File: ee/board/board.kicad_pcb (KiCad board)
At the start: 4 copper layers, 87.1 x 53.4 mm, 103 parts, among them J3 USB_A, J4 Conn_01x08_Pin, J5 Conn_01x10_Pin, J6 Conn_Coaxial, J8 HR911105A, U1 RTL8201F, U2 RTL8723DS, U6 USBLC6-2SC6, Y1 Crystal_GND24_Small

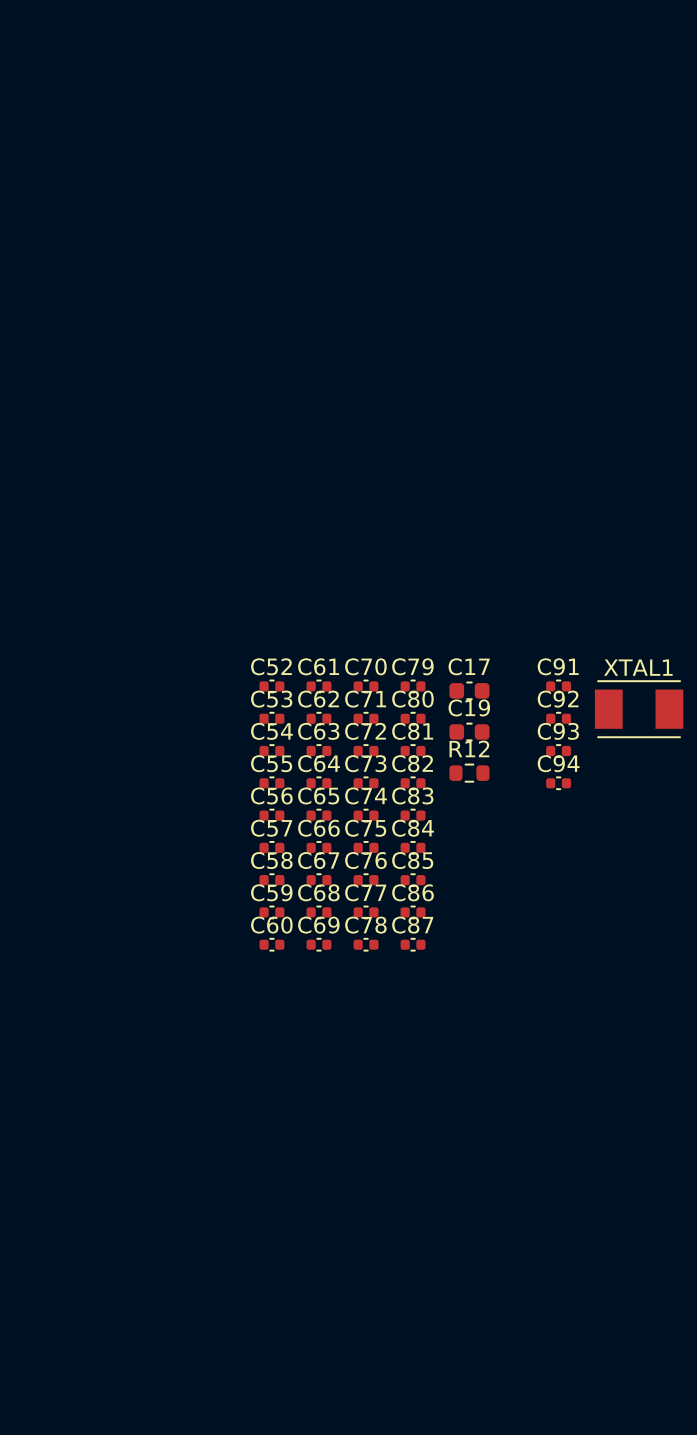
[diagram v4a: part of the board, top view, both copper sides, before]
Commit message: Added the footprints into the design.
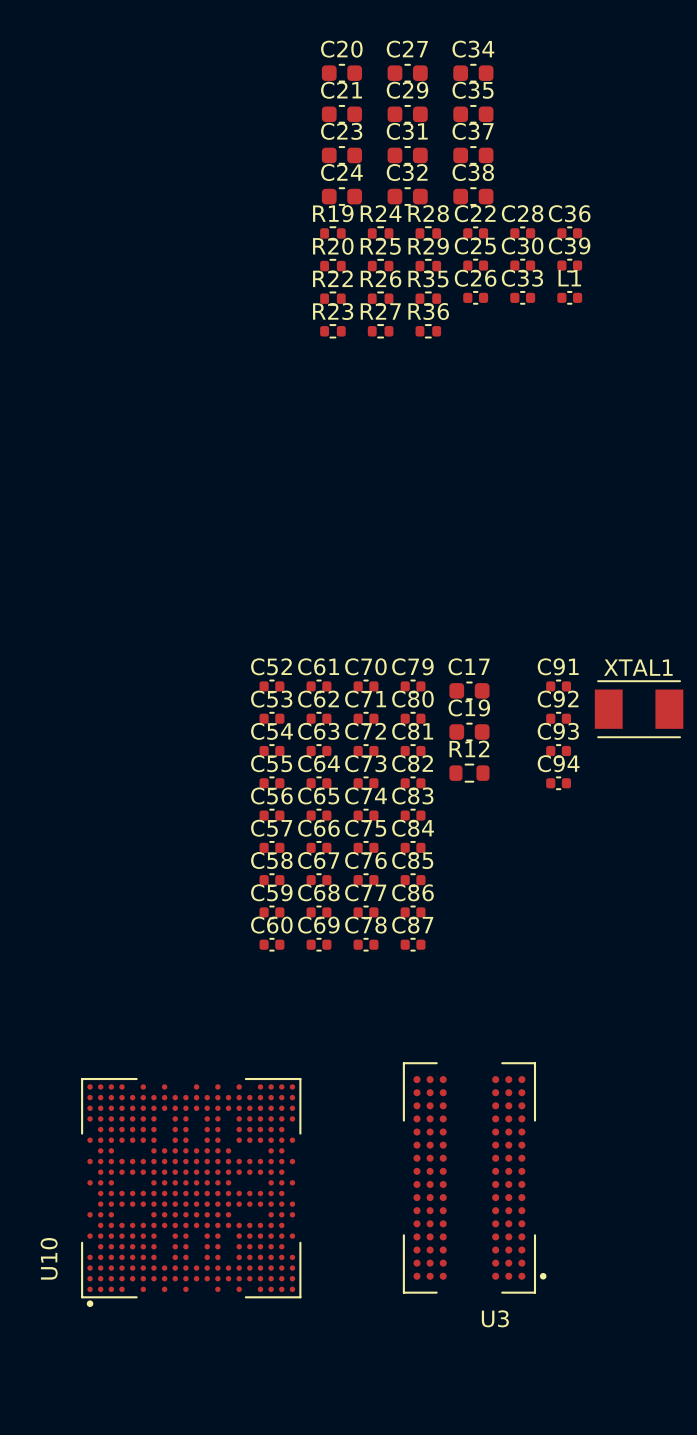
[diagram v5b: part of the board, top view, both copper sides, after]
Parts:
- added C20: 22uF, Capacitor_SMD:C_0603_1608Metric, F.Cu at (72.7, 64.9)
- added C21: 10uF, Capacitor_SMD:C_0603_1608Metric, F.Cu at (72.7, 67.4)
- added C22: 0.1uF, Capacitor_SMD:C_0402_1005Metric, F.Cu at (80.9, 74.7)
- added C23: 10uF, Capacitor_SMD:C_0603_1608Metric, F.Cu at (72.7, 69.9)
- added C24: 10uF, Capacitor_SMD:C_0603_1608Metric, F.Cu at (72.7, 72.4)
- added C25: 0.1uF, Capacitor_SMD:C_0402_1005Metric, F.Cu at (80.9, 76.6)
- added C26: 0.1uF, Capacitor_SMD:C_0402_1005Metric, F.Cu at (80.9, 78.6)
- added C27: 10uF, Capacitor_SMD:C_0603_1608Metric, F.Cu at (76.7, 64.9)
- added C28: 0.1uF, Capacitor_SMD:C_0402_1005Metric, F.Cu at (83.8, 74.7)
- added C29: 22uF, Capacitor_SMD:C_0603_1608Metric, F.Cu at (76.7, 67.4)
- added C30: 0.1uF, Capacitor_SMD:C_0402_1005Metric, F.Cu at (83.8, 76.6)
- added C31: 22uF, Capacitor_SMD:C_0603_1608Metric, F.Cu at (76.7, 69.9)
- added C32: 22uF, Capacitor_SMD:C_0603_1608Metric, F.Cu at (76.7, 72.4)
- added C33: 0.1uF, Capacitor_SMD:C_0402_1005Metric, F.Cu at (83.8, 78.6)
- added C34: 22uF, Capacitor_SMD:C_0603_1608Metric, F.Cu at (80.7, 64.9)
- added C35: 22uF, Capacitor_SMD:C_0603_1608Metric, F.Cu at (80.7, 67.4)
- added C36: 0.1uF, Capacitor_SMD:C_0402_1005Metric, F.Cu at (86.6, 74.7)
- added C37: 22uF, Capacitor_SMD:C_0603_1608Metric, F.Cu at (80.7, 69.9)
- added C38: 22uF, Capacitor_SMD:C_0603_1608Metric, F.Cu at (80.7, 72.4)
- added C39: 0.1uF, Capacitor_SMD:C_0402_1005Metric, F.Cu at (86.6, 76.6)
- added L1: 3.3uH, Capacitor_SMD:C_0402_1005Metric, F.Cu at (86.6, 78.6)
- added R19: 10k, Resistor_SMD:R_0402_1005Metric, F.Cu at (72.2, 74.7)
- added R20: 590R, Resistor_SMD:R_0402_1005Metric, F.Cu at (72.2, 76.7)
- added R22: 10k, Resistor_SMD:R_0402_1005Metric, F.Cu at (72.2, 78.7)
- added R23: 31.6k, Resistor_SMD:R_0402_1005Metric, F.Cu at (72.2, 80.6)
- added R24: 10k, Resistor_SMD:R_0402_1005Metric, F.Cu at (75.1, 74.7)
- added R25: 10k, Resistor_SMD:R_0402_1005Metric, F.Cu at (75.1, 76.7)
- added R26: 8.66K, Resistor_SMD:R_0402_1005Metric, F.Cu at (75.1, 78.7)
- added R27: 10k, Resistor_SMD:R_0402_1005Metric, F.Cu at (75.1, 80.6)
- added R28: 10k, Resistor_SMD:R_0402_1005Metric, F.Cu at (78.0, 74.7)
- added R29: 10k, Resistor_SMD:R_0402_1005Metric, F.Cu at (78.0, 76.7)
- added R35: 12.4K, Resistor_SMD:R_0402_1005Metric, F.Cu at (78.0, 78.7)
- added R36: 10k, Resistor_SMD:R_0402_1005Metric, F.Cu at (78.0, 80.6)
- added U10: ALLWINNER_D1, allwinnder_d1:BGA337C65P20X20_1300X1300X133, F.Cu at (63.5, 132.9)
- added U3: MT41K256M16TW-107_P, ddr3:BGA96C80P9X16_1400X800X120, F.Cu at (80.5, 132.3)
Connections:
- net /MPU/PG12 renamed /MPU/PG10

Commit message: Leftover stuff
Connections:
- net /1W renamed /Flipper_1W
- net /B2 renamed /Flipper_B2
- net /B3 renamed /Flipper_B3
- net /C0 renamed /Flipper_C0
- net /C1 renamed /Flipper_C1
- net /C3 renamed /Flipper_C3
- net /SIO renamed /Flipper_SIO
- net /SWC renamed /Flipper_SWC
- J4 pad 2: /MPU/A7 -> /Flipper_A7
- J4 pad 3: /MPU/A6 -> /Flipper_A6
- J4 pad 4: /MPU/A4 -> /Flipper_A4
- JP1 pad 2: /MPU/PG18 -> /WiFi/PG18
- R14 pad 1: /MPU/PG11 -> /WiFi/PG11
- R16 pad 1: /MPU/PG7 -> /WiFi/PG7
- R17 pad 1: /MPU/PG6 -> /WiFi/PG6
- R18 pad 2: /MPU/PG10 -> /WiFi/PG10
- R4 pad 2: /MPU/PG16 -> /WiFi/PG16
- RN1 pad 1: /MPU/PG3 -> /WiFi/PG3
- RN1 pad 2: /MPU/PG2 -> /WiFi/PG2
- RN1 pad 3: /MPU/PG0 -> /WiFi/PG0
- RN1 pad 4: /MPU/PG1 -> /WiFi/PG1
- RN2 pad 1: /MPU/PG5 -> /WiFi/PG5
- RN2 pad 2: /MPU/PG4 -> /WiFi/PG4
- RN2 pad 3: /MPU/PG10 -> /WiFi/PG10
- RN2 pad 4: /MPU/PG10 -> /WiFi/PG10
- U10 pad D5: /MPU/PG10 -> /MPU/PG12
- U2 pad 12: /MPU/PG10 -> /WiFi/PG10
- U2 pad 13: /MPU/PG10 -> /WiFi/PG10
- U2 pad 14: /MPU/PG4 -> /WiFi/PG4
- U2 pad 15: /MPU/PG5 -> /WiFi/PG5
- U2 pad 16: /MPU/PG1 -> /WiFi/PG1
- U2 pad 17: /MPU/PG0 -> /WiFi/PG0
- U2 pad 18: /MPU/PG2 -> /WiFi/PG2
- U2 pad 19: /MPU/PG3 -> /WiFi/PG3
- U2 pad 41: /MPU/PG9 -> /WiFi/PG9
- U2 pad 44: /MPU/PG8 -> /WiFi/PG8
- U2 pad 6: /MPU/PG16 -> /WiFi/PG16
- U2 pad 7: /MPU/PG17 -> /WiFi/PG17
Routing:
- net /WiFi/PG10: track 0.00 -> 53.5 mm, vias 0 -> 4
- net /MPU/PG10: track 53.5 -> 0.00 mm, vias 4 -> 0
- net /WiFi/PG4: track 0.00 -> 30.0 mm, vias 0 -> 2
- net /MPU/PG4: track 30.0 -> 0.00 mm, vias 2 -> 0
- net /WiFi/PG1: track 0.00 -> 28.5 mm, vias 0 -> 2
- net /MPU/PG1: track 28.5 -> 0.00 mm, vias 2 -> 0
- net /WiFi/PG5: track 0.00 -> 28.0 mm, vias 0 -> 2
- net /MPU/PG5: track 28.0 -> 0.00 mm, vias 2 -> 0
- net /WiFi/PG6: track 0.00 -> 27.8 mm, vias 0 -> 2
- net /MPU/PG6: track 27.8 -> 0.00 mm, vias 2 -> 0
- net /WiFi/PG3: track 0.00 -> 27.2 mm, vias 0 -> 2
- net /MPU/PG3: track 27.2 -> 0.00 mm, vias 2 -> 0
- net /WiFi/PG2: track 0.00 -> 26.9 mm, vias 0 -> 2
- net /MPU/PG2: track 26.9 -> 0.00 mm, vias 2 -> 0
- net /WiFi/PG0: track 0.00 -> 26.9 mm, vias 0 -> 2
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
